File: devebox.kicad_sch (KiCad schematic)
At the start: 28 parts, among them J1 ST-LINK, J2 USB, J3 Right Header, J4 Left Header, SW1 RESET SW, U1 STM32H743VITx, Y1 25MHZ

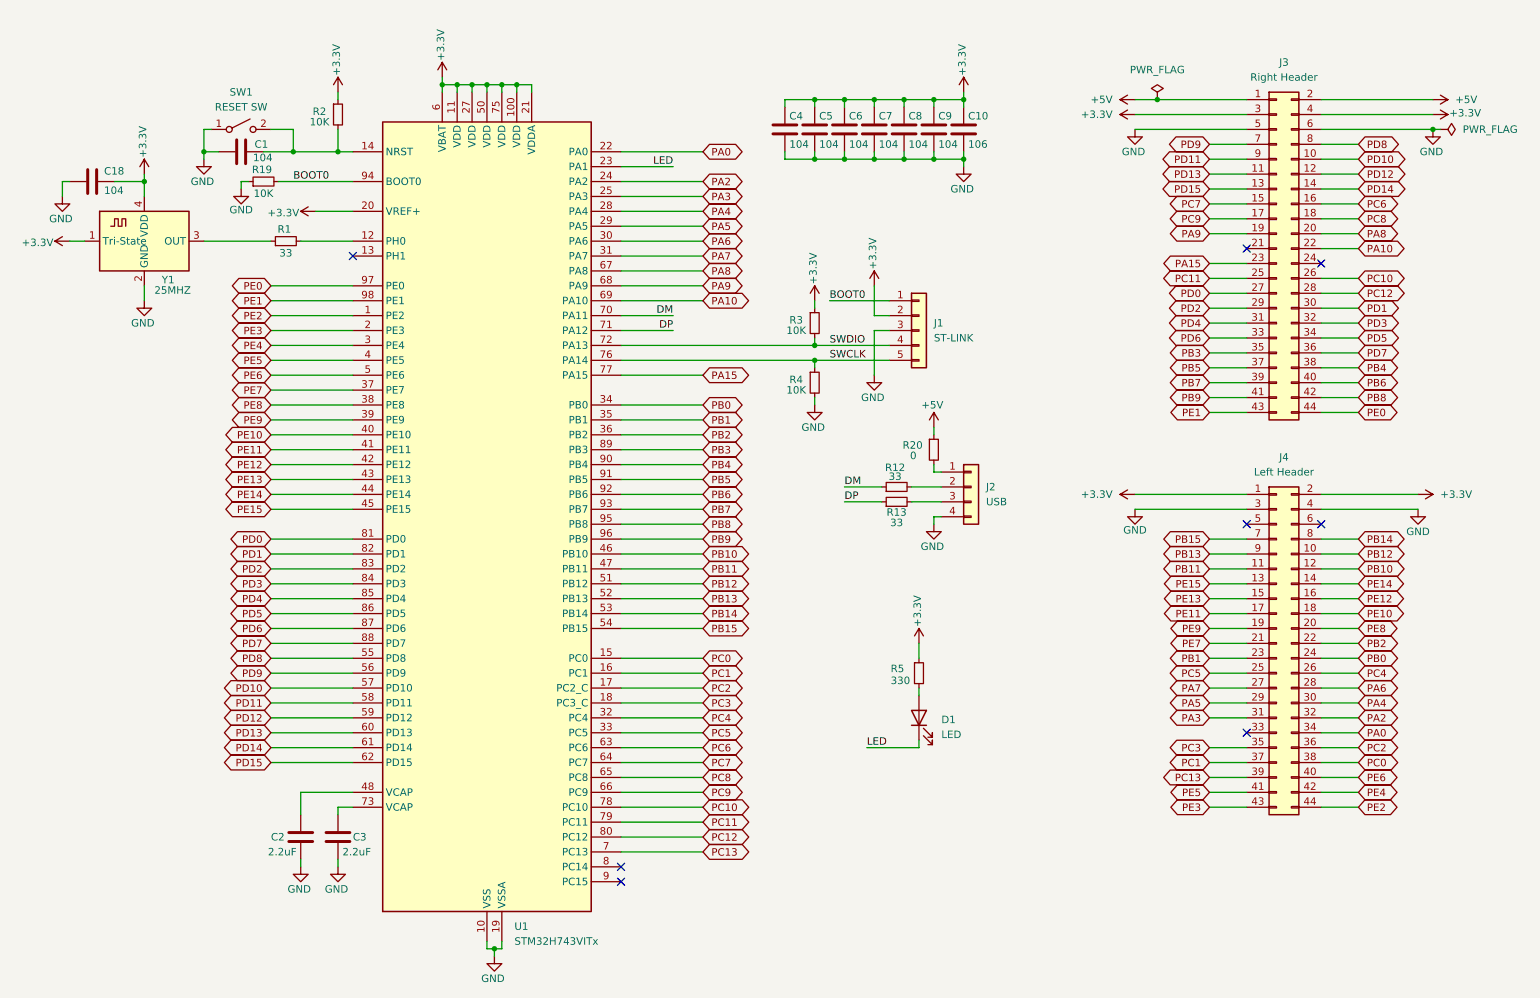
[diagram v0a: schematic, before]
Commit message: start of new board with STM32H743VIT6 included
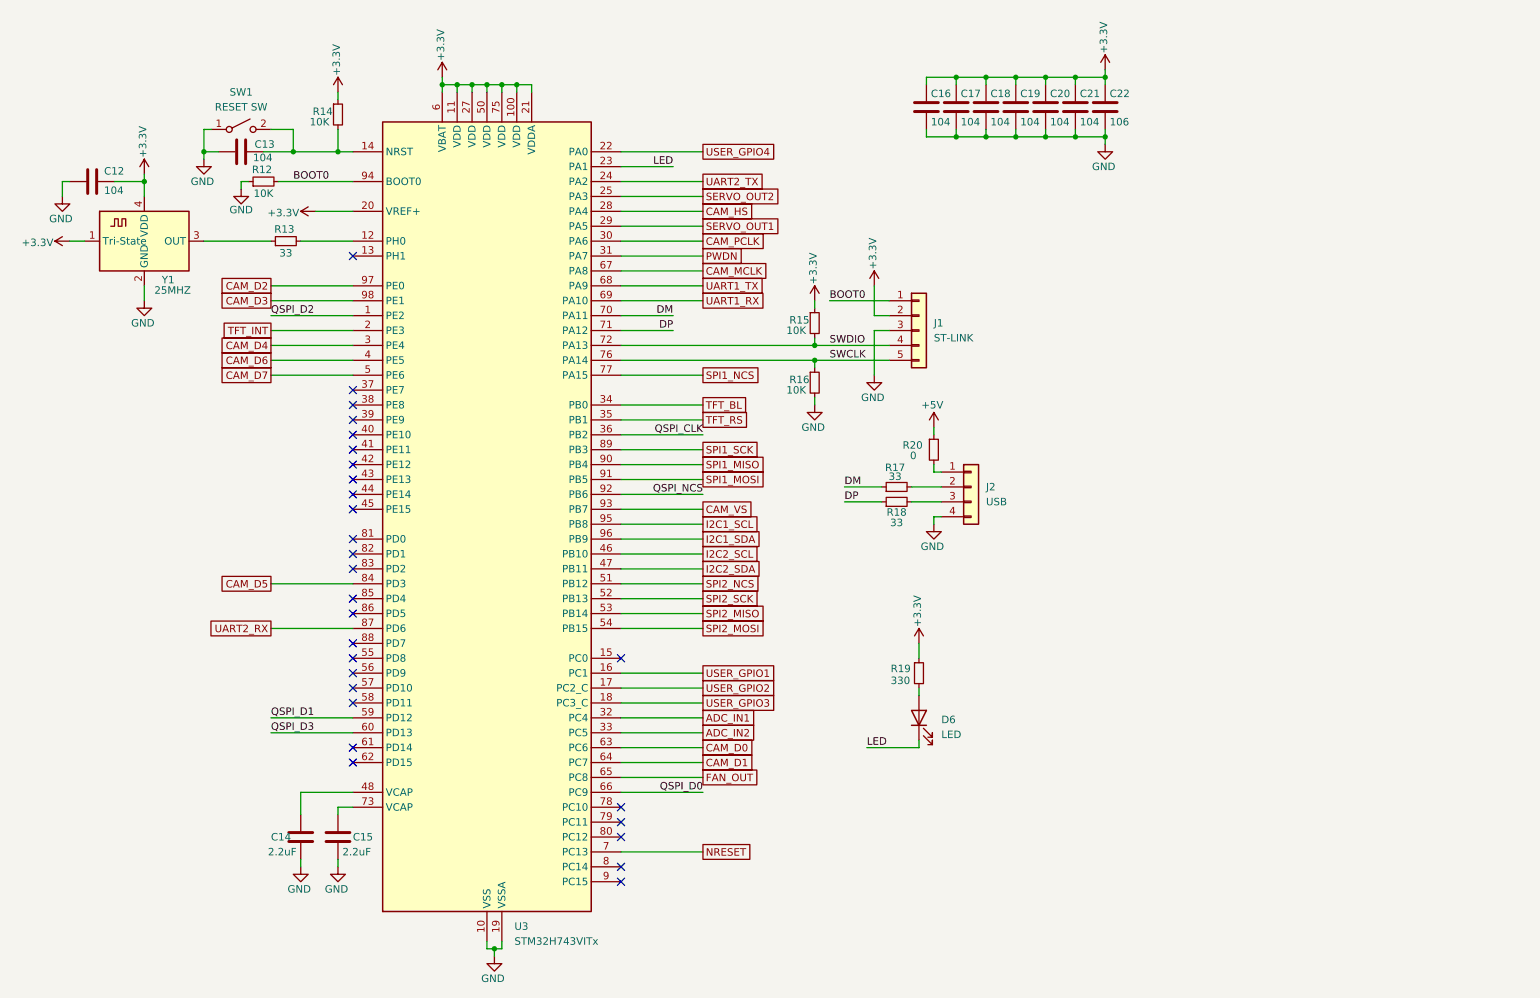
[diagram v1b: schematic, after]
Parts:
- removed J3: Right Header, Connector_PinHeader_2.54mm:PinHeader_2x22_P2.54mm_Vertical, symbol LM2676S-3.3_NOPB:Conn_02x22_Odd_Even
- removed J4: Left Header, Connector_PinHeader_2.54mm:PinHeader_2x22_P2.54mm_Vertical, symbol LM2676S-3.3_NOPB:Conn_02x22_Odd_Even
- renumbered C18 to C12, C1 to C13, C2 to C14, C3 to C15, C4 to C16, C5 to C17, C6 to C18, C7 to C19, C8 to C20, C9 to C21, C10 to C22, D1 to D6, R19 to R12, R1 to R13, R2 to R14, R3 to R15, R4 to R16, R12 to R17, R13 to R18, R5 to R19, U1 to U3
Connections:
- net PA0 renamed USER_GPIO4
- net PA10 renamed UART1_RX
- net PA15 renamed SPI1_NCS
- net PA2 renamed UART2_TX
- net PA3 renamed SERVO_OUT2
- net PA4 renamed CAM_HS
- net PA5 renamed SERVO_OUT1
- net PA6 renamed CAM_PCLK
- net PA7 renamed PWDN
- net PA8 renamed CAM_MCLK
- net PA9 renamed UART1_TX
- net PB0 renamed TFT_BL
- net PB1 renamed TFT_RS
- net PB10 renamed I2C2_SCL
- net PB11 renamed I2C2_SDA
- net PB12 renamed SPI2_NCS
- net PB13 renamed SPI2_SCK
- net PB14 renamed SPI2_MISO
- net PB15 renamed SPI2_MOSI
- net PB2 renamed QSPI_CLK
- net PB3 renamed SPI1_SCK
- net PB4 renamed SPI1_MISO
- net PB5 renamed SPI1_MOSI
- net PB6 renamed QSPI_NCS
- net PB7 renamed CAM_VS
- net PB8 renamed I2C1_SCL
- net PB9 renamed I2C1_SDA
- net PC0: no longer names the net of U3.15 (PC0)
- net PC1 renamed USER_GPIO1
- net PC10: no longer names the net of U3.78 (PC10)
- net PC11: no longer names the net of U3.79 (PC11)
- net PC12: no longer names the net of U3.80 (PC12)
- net PC13 renamed NRESET
- net PC2 renamed USER_GPIO2
- net PC3 renamed USER_GPIO3
- net PC4 renamed ADC_IN1
- net PC5 renamed ADC_IN2
- net PC6 renamed CAM_D0
- net PC7 renamed CAM_D1
- net PC8 renamed FAN_OUT
- net PC9 renamed QSPI_D0
- net PD0: no longer names the net of U3.81 (PD0)
- net PD1: no longer names the net of U3.82 (PD1)
- net PD10: no longer names the net of U3.57 (PD10)
- net PD11: no longer names the net of U3.58 (PD11)
- net PD12 renamed QSPI_D1
- net PD13 renamed QSPI_D3
- net PD14: no longer names the net of U3.61 (PD14)
- net PD15: no longer names the net of U3.62 (PD15)
- net PD2: no longer names the net of U3.83 (PD2)
- net PD3 renamed CAM_D5
- net PD4: no longer names the net of U3.85 (PD4)
- net PD5: no longer names the net of U3.86 (PD5)
- net PD6 renamed UART2_RX
- net PD7: no longer names the net of U3.88 (PD7)
- net PD8: no longer names the net of U3.55 (PD8)
- net PD9: no longer names the net of U3.56 (PD9)
- net PE0 renamed CAM_D2
- net PE1 renamed CAM_D3
- net PE10: no longer names the net of U3.40 (PE10)
- net PE11: no longer names the net of U3.41 (PE11)
- net PE12: no longer names the net of U3.42 (PE12)
- net PE13: no longer names the net of U3.43 (PE13)
- net PE14: no longer names the net of U3.44 (PE14)
- net PE15: no longer names the net of U3.45 (PE15)
- net PE2 renamed QSPI_D2
- net PE3 renamed TFT_INT
- net PE4 renamed CAM_D4
- net PE5 renamed CAM_D6
- net PE6 renamed CAM_D7
- net PE7: no longer names the net of U3.37 (PE7)
- net PE8: no longer names the net of U3.38 (PE8)
- net PE9: no longer names the net of U3.39 (PE9)
- no-connect marks 8 -> 28
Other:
- moved on the sheet: C16, C17, C18, C19, C20, C21, C22

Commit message: snapshot
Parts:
- added U4: W25Q128, PCM_JLCPCB:SOIC-8_L5.3-W5.3-P1.27-LS8.0-BL, symbol EggClassifier:16MByte,_SPI
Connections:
- net +3.3V: now also U4.8 (VCC)
- net GND: now also U4.4 (GND)
- net QSPI_CLK: now also U4.6 (CLK)
- net QSPI_D0: now also U4.5 (DI)
- net QSPI_D1: now also U4.2 (DO)
- net QSPI_D2: now also U4.3 (IO2)
- net QSPI_D3: now also U4.7 (IO3)
- net QSPI_NCS: now also U4.1 (CS#)
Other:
- moved on the sheet: C16

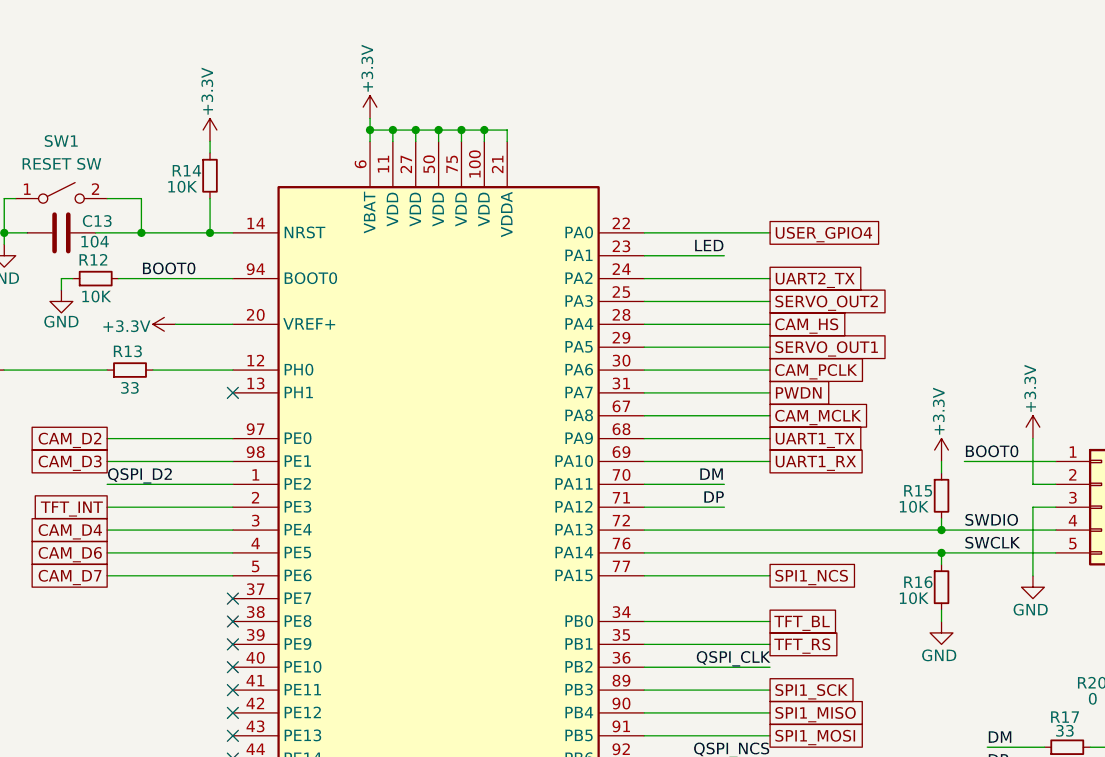
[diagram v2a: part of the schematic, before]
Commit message: update R11 value to 4.7K
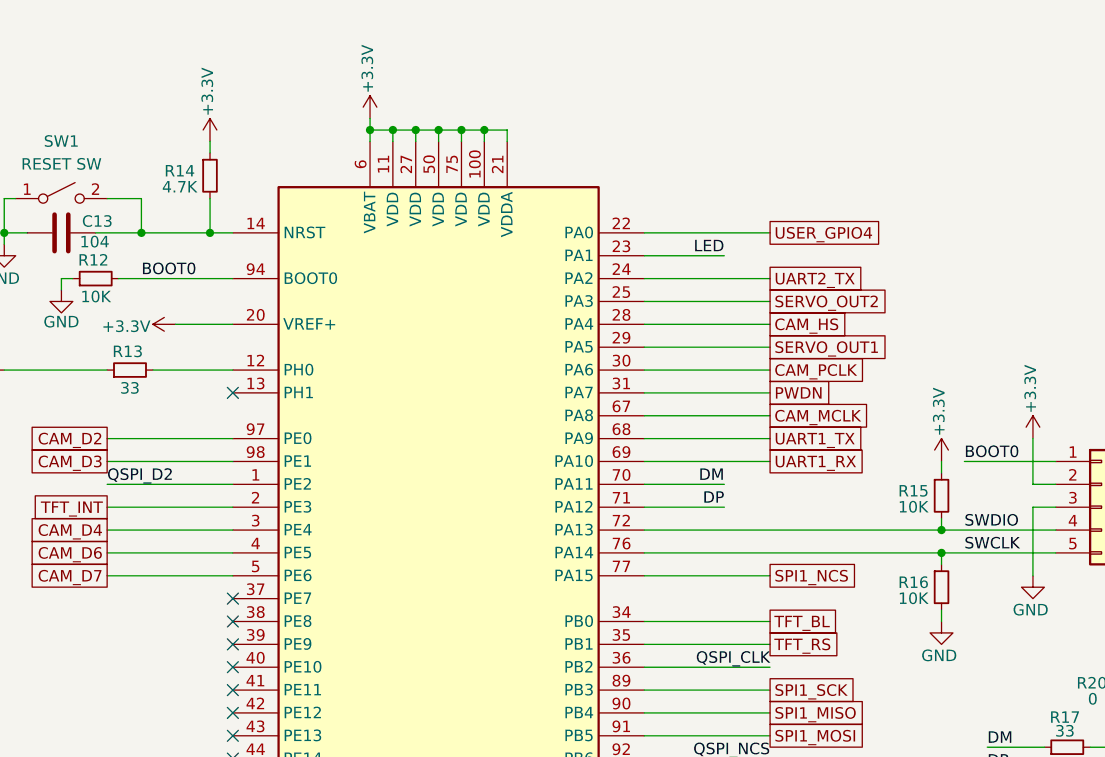
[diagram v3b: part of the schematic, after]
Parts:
- R14: value 10K -> 4.7K
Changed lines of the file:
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@@
 		(dnp no)
 		(property "Reference" "R16"
-			(at 149.352 76.962 0)
+			(at 148.844 76.962 0)
 			(effects
 				(font
@@
 		(dnp no)
 		(property "Reference" "R15"
-			(at 149.352 66.802 0)
+			(at 148.844 66.802 0)
 			(effects
 				(font
@@
 		(dnp no)
 		(property "Reference" "R14"
-			(at 68.072 31.242 0)
-			(effects
-				(font
-					(size 1.27 1.27)
-				)
-				(justify left)
-			)
-		)
-		(property "Value" "10K"
-			(at 67.564 33.02 0)
-			(effects
-				(font
+			(at 67.31 31.242 0)
+			(effects
+				(font
+					(size 1.27 1.27)
+				)
+				(justify left)
+			)
+		)
+		(property "Value" "4.7K"
+			(at 67.056 33.02 0)
+			(effects
+				(font

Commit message: snapshot prior to merge
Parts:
- C12, C13, C14, C15, C16, C17, C18, C19, C20, C21, C22: symbol LM2676S-3.3_NOPB:C -> EggClassifier:C
- D6: symbol LM2676S-3.3_NOPB:LED -> EggClassifier:LED
- J1: symbol LM2676S-3.3_NOPB:Conn_01x05 -> EggClassifier:Conn_01x05
- J2: symbol LM2676S-3.3_NOPB:Conn_01x04_1 -> EggClassifier:Conn_01x04_1
- R12, R13, R14, R15, R16, R17, R18, R19, R20: symbol LM2676S-3.3_NOPB:R_Small -> EggClassifier:R_Small
- SW1: symbol LM2676S-3.3_NOPB:SPST_Momentary_4.6x2.8mm -> EggClassifier:SPST_Momentary_4.6x2.8mm
- U3: symbol LM2676S-3.3_NOPB:STM32H743VITx -> EggClassifier:STM32H743VITx
- Y1: symbol LM2676S-3.3_NOPB:ASCO -> EggClassifier:ASCO
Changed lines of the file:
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@@
 	)
 	(symbol
-		(lib_id "LM2676S-3.3_NOPB:R_Small")
+		(lib_id "EggClassifier:R_Small")
 		(at 167.64 95.25 90)
 		(unit 1)
@@
 	)
 	(symbol
-		(lib_id "LM2676S-3.3_NOPB:C")
+		(lib_id "EggClassifier:C")
 		(at 248.92 82.55 90)
 		(unit 1)
@@
 	)
 	(symbol
-		(lib_id "LM2676S-3.3_NOPB:C")
+		(lib_id "EggClassifier:C")
 		(at 72.39 154.94 0)
 		(unit 1)
@@
 	)
 	(symbol
-		(lib_id "LM2676S-3.3_NOPB:R_Small")
+		(lib_id "EggClassifier:R_Small")
 		(at 153.67 77.47 0)
 		(unit 1)
@@
 	)
 	(symbol
-		(lib_id "LM2676S-3.3_NOPB:C")
+		(lib_id "EggClassifier:C")
 		(at 30.48 43.18 270)
 		(unit 1)
@@
 	)
 	(symbol
-		(lib_id "LM2676S-3.3_NOPB:R_Small")
+		(lib_id "EggClassifier:R_Small")
 		(at 171.45 127 0)
 		(unit 1)
@@
 	)
 	(symbol
-		(lib_id "LM2676S-3.3_NOPB:R_Small")
+		(lib_id "EggClassifier:R_Small")
 		(at 63.5 53.34 90)
 		(unit 1)
@@
 	)
 	(symbol
-		(lib_id "LM2676S-3.3_NOPB:C")
+		(lib_id "EggClassifier:C")
 		(at 198.12 30.48 0)
 		(unit 1)
@@
 	)
 	(symbol
-		(lib_id "LM2676S-3.3_NOPB:C")
+		(lib_id "EggClassifier:C")
 		(at 55.88 38.1 270)
 		(unit 1)
@@
 	)
 	(symbol
-		(lib_id "LM2676S-3.3_NOPB:R_Small")
+		(lib_id "EggClassifier:R_Small")
 		(at 153.67 67.31 0)
 		(unit 1)
@@
 	)
 	(symbol
-		(lib_id "LM2676S-3.3_NOPB:STM32H743VITx")
+		(lib_id "EggClassifier:STM32H743VITx")
 		(at 97.79 101.6 0)
 		(unit 1)
@@
 	)
 	(symbol
-		(lib_id "LM2676S-3.3_NOPB:C")
+		(lib_id "EggClassifier:C")
 		(at 187.96 30.48 0)
 		(unit 1)
@@
 	)
 	(symbol
-		(lib_id "LM2676S-3.3_NOPB:ASCO")
+		(lib_id "EggClassifier:ASCO")
 		(at 39.37 53.34 0)
 		(unit 1)
@@
 	)
 	(symbol
-		(lib_id "LM2676S-3.3_NOPB:R_Small")
+		(lib_id "EggClassifier:R_Small")
 		(at 167.64 97.79 90)
 		(unit 1)
@@
 	)
 	(symbol
-		(lib_id "LM2676S-3.3_NOPB:C")
+		(lib_id "EggClassifier:C")
 		(at 177.8 30.48 0)
 		(unit 1)
@@
 	)
 	(symbol
-		(lib_id "LM2676S-3.3_NOPB:SPST_Momentary_4.6x2.8mm")
+		(lib_id "EggClassifier:SPST_Momentary_4.6x2.8mm")
 		(at 55.88 34.29 0)
 		(unit 1)
@@
 	(symbol
 		(lib_name "Conn_01x04_1")
-		(lib_id "LM2676S-3.3_NOPB:Conn_01x04_1")
+		(lib_id "EggClassifier:Conn_01x04_1")
 		(at 180.34 95.25 0)
 		(unit 1)
@@
 	)
 	(symbol
-		(lib_id "LM2676S-3.3_NOPB:C")
+		(lib_id "EggClassifier:C")
 		(at 66.04 154.94 0)
 		(unit 1)
@@
 	)
 	(symbol
-		(lib_id "LM2676S-3.3_NOPB:R_Small")
+		(lib_id "EggClassifier:R_Small")
 		(at 59.69 43.18 90)
 		(unit 1)
@@
 	)
 	(symbol
-		(lib_id "LM2676S-3.3_NOPB:Conn_01x05")
+		(lib_id "EggClassifier:Conn_01x05")
 		(at 171.45 68.58 0)
 		(unit 1)
@@
 	)
 	(symbol
-		(lib_id "LM2676S-3.3_NOPB:C")
+		(lib_id "EggClassifier:C")
 		(at 203.2 30.48 0)
 		(unit 1)
@@
 	)
 	(symbol
-		(lib_id "LM2676S-3.3_NOPB:LED")
+		(lib_id "EggClassifier:LED")
 		(at 171.45 134.62 90)
 		(unit 1)
@@
 	)
 	(symbol
-		(lib_id "LM2676S-3.3_NOPB:R_Small")
+		(lib_id "EggClassifier:R_Small")
 		(at 72.39 31.75 0)
 		(unit 1)
@@
 	)
 	(symbol
-		(lib_id "LM2676S-3.3_NOPB:R_Small")
+		(lib_id "EggClassifier:R_Small")
 		(at 173.99 88.9 0)
 		(unit 1)
@@
 	)
 	(symbol
-		(lib_id "LM2676S-3.3_NOPB:C")
+		(lib_id "EggClassifier:C")
 		(at 182.88 30.48 0)
 		(unit 1)
@@
 	)
 	(symbol
-		(lib_id "LM2676S-3.3_NOPB:C")
+		(lib_id "EggClassifier:C")
 		(at 193.04 30.48 0)
 		(unit 1)

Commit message: sync from JLCPCB
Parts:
- R12, R15, R16: value 10K -> 4.7K
- R19: value 330 -> 4.7K
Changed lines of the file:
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@@
 	)
 	(junction
-		(at 173.99 83.82)
-		(diameter 0)
-		(color 0 0 0 0)
-	)
-	(junction
 		(at 72.39 38.1)
 		(diameter 0)
@@
 	(wire
 		(pts
-			(xy 173.99 82.55) (xy 173.99 83.82)
-		)
-		(stroke
-			(width 0)
-			(type default)
-		)
-	)
-	(wire
-		(pts
 			(xy 193.04 34.29) (xy 193.04 35.56)
 		)
@@
 	(wire
 		(pts
-			(xy 173.99 83.82) (xy 175.26 83.82)
-		)
-		(stroke
-			(width 0)
-			(type default)
-		)
-	)
-	(wire
-		(pts
 			(xy 120.65 50.8) (xy 134.62 50.8)
 		)
@@
 	(wire
 		(pts
+			(xy 173.99 82.55) (xy 173.99 86.36)
+		)
+		(stroke
+			(width 0)
+			(type default)
+		)
+	)
+	(wire
+		(pts
 			(xy 64.77 38.1) (xy 72.39 38.1)
 		)
@@
 	(wire
 		(pts
-			(xy 173.99 83.82) (xy 173.99 86.36)
-		)
-		(stroke
-			(width 0)
-			(type default)
-		)
-	)
-	(wire
-		(pts
 			(xy 97.79 172.72) (xy 97.79 173.99)
 		)
@@
 			)
 		)
-		(property "Value" "10K"
-			(at 148.844 78.74 0)
+		(property "Value" "4.7K"
+			(at 148.082 78.74 0)
 			(effects
 				(font
@@
 			)
 		)
-		(property "Value" "330"
-			(at 166.624 128.27 0)
+		(property "Value" "4.7K"
+			(at 165.862 128.016 0)
 			(effects
 				(font
@@
 			)
 		)
-		(property "Value" "10K"
-			(at 148.844 68.58 0)
+		(property "Value" "4.7K"
+			(at 148.082 68.58 0)
 			(effects
 				(font
@@
 	)
 	(symbol
-		(lib_id "LM2676S-3.3_NOPB:PWR_FLAG")
-		(at 175.26 83.82 270)
-		(unit 1)
-		(exclude_from_sim no)
-		(in_bom yes)
-		(on_board yes)
-		(dnp no)
-		(fields_autoplaced yes)
-		(property "Reference" "#FLG02"
-			(at 177.165 83.82 0)
-			(effects
-				(font
-					(size 1.27 1.27)
-				)
-				(hide yes)
-			)
-		)
-		(property "Value" "PWR_FLAG"
-			(at 179.07 83.8199 90)
-			(effects
-				(font
-					(size 1.27 1.27)
-				)
-				(justify left)
-			)
-		)
-		(property "Footprint" ""
-			(at 175.26 83.82 0)
-			(effects
-				(font
-					(size 1.27 1.27)
-				)
-				(hide yes)
-			)
-		)
-		(property "Datasheet" "~"
-			(at 175.26 83.82 0)
-			(effects
-				(font
-					(size 1.27 1.27)
-				)
-				(hide yes)
-			)
-		)
-		(property "Description" "Special symbol for telling ERC where power comes from"
-			(at 175.26 83.82 0)
-			(effects
-				(font
-					(size 1.27 1.27)
-				)
-				(hide yes)
-			)
-		)
-		(pin "1"
-		)
-		(instances
-			(project "EggClassifier"
-				(path "/1c72d2eb-7fb1-49fe-a026-e817f5a7ec43/fdbe9d4c-6ebe-4e90-8f03-e4455b1d326a"
-					(reference "#FLG02")
-					(unit 1)
-				)
-			)
-		)
-	)
-	(symbol
 		(lib_id "EggClassifier:C")
 		(at 177.8 30.48 0)
@@
 			)
 		)
-		(property "Value" "10K"
+		(property "Value" "4.7K"
 			(at 59.69 45.212 90)
 			(effects
